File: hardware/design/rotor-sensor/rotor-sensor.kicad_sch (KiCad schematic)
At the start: 48 parts, among them J1 Conn_ARM_SWD_TagConnect_TC203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, J2 Conn_01x06, U4 ATSAMD21E18A-MUT, U5 TLIN1028-Q1, U600 BMI088

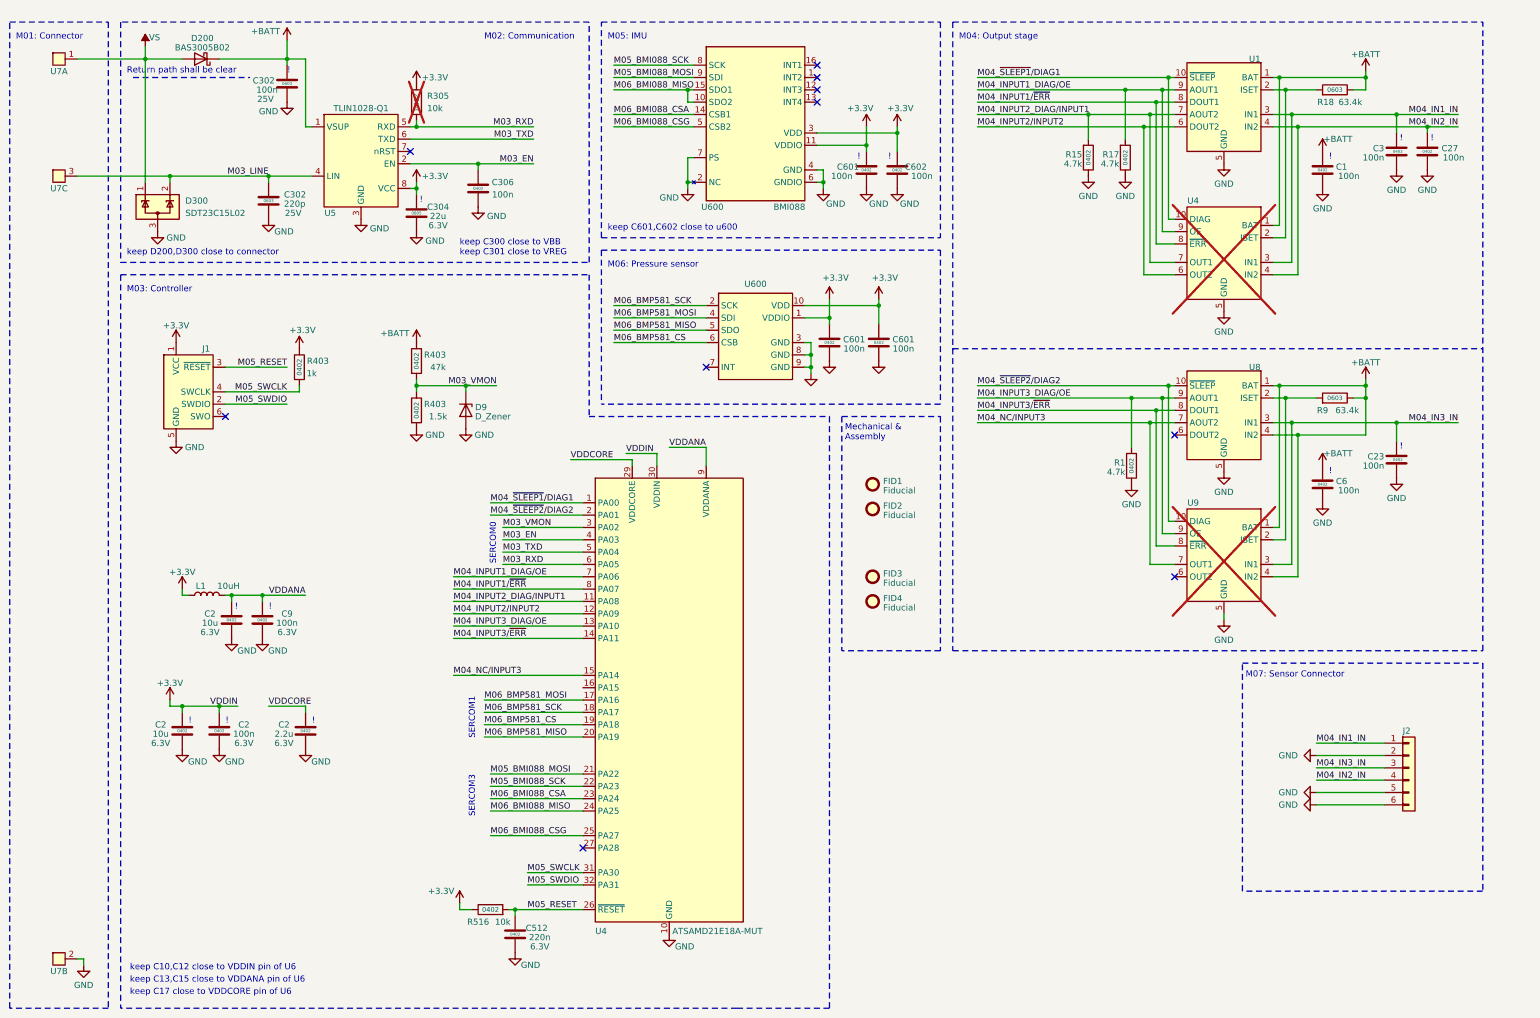
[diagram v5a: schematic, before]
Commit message: FInal ordered hardware
New 3pin connector
Extra 2pin connector for cadence measurement
No 3pin sensor variant
DC/DC converter for MCU
Pressure sensor
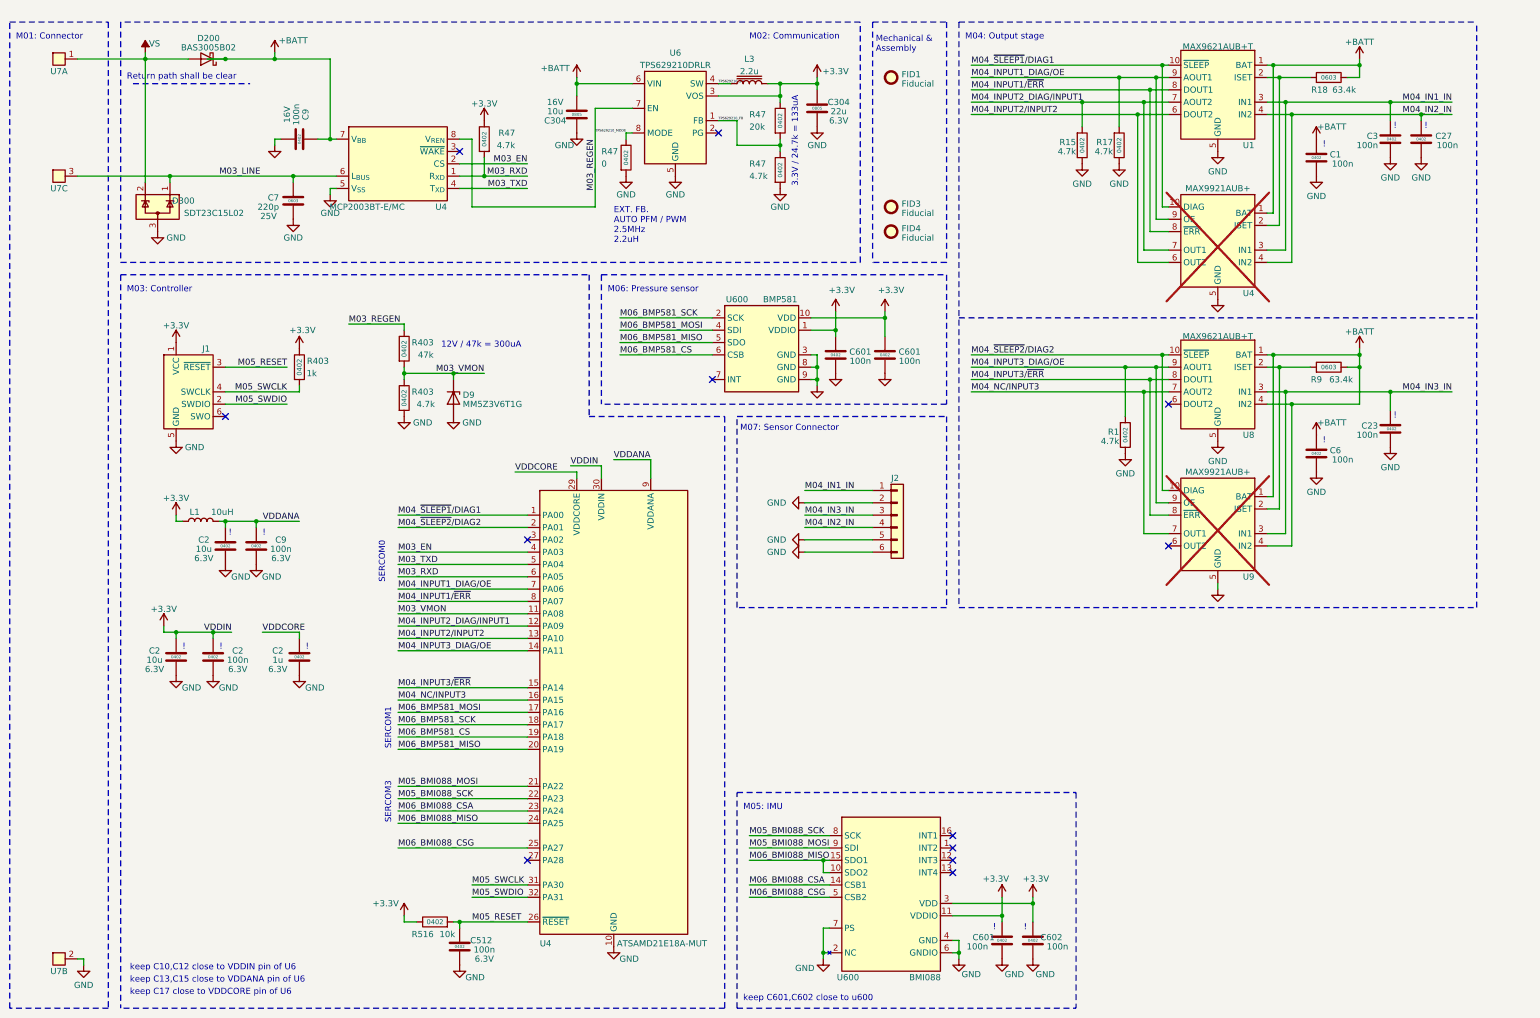
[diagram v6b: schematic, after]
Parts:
- removed C302: 100n, Capacitor_SMD:C_0603_1608Metric, symbol Device:C
- removed C302: 220p, Capacitor_SMD:C_0603_1608Metric, symbol Device:C
- removed C304: 22u, Capacitor_SMD:C_0805_2012Metric, symbol Device:C
- removed C306: 100n, Capacitor_SMD:C_0402_1005Metric, symbol Device:C
- removed FID2: Fiducial, Fiducial:Fiducial_0.5mm_Mask1mm, symbol Mechanical:Fiducial
- removed R305: 10k, Resistor_SMD:R_0402_1005Metric, symbol Device:R
- removed U5: TLIN1028-Q1, Package_SON:Texas_S-PVSON-N8, symbol local_symbols:TLIN1028-Q1
- added C304: 22u, Capacitor_SMD:C_0805_2012Metric, symbol Device:C
- added C304: 10u, Capacitor_SMD:C_0805_2012Metric, symbol Device:C
- added C7: 220p, Capacitor_SMD:C_0603_1608Metric, symbol Device:C
- added C9: 100n, Capacitor_SMD:C_0402_1005Metric, symbol Device:C
- added L3: 2.2u, Inductor_SMD:L_Coilcraft_LPS3010, symbol Device:L_Iron
- added R47: 0, Resistor_SMD:R_0402_1005Metric, symbol Device:R
- added R47: 20k, Resistor_SMD:R_0402_1005Metric, symbol Device:R
- added R47 (x2): 4.7k, Resistor_SMD:R_0402_1005Metric, symbol Device:R
- added U4: MCP2003BT-E/MC, Package_DFN_QFN:DFN-8-1EP_3x2mm_P0.5mm_EP1.7x1.4mm, symbol local:MCP2003
- added U6: TPS629210DRLR, Package_TO_SOT_SMD:SOT-583-8, symbol local_symbols:TPS629210
- C2: value 2.2u -> 1u
- C512: value 220n -> 100n
- D9: value D_Zener -> MM5Z3V6T1G
- R403: value 1.5k -> 4.7k
- U1, U8: value ~ -> MAX9621AUB+T
- U4, U9: value ~ -> MAX9921AUB+
- U600: value ~ -> BMP581
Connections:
- net +3.3V: now also C304.1, L3.2, R47.1, R47.1, U6.3 (VOS)
- net +BATT: now also C304.2, C9.2, U4.7 (V_{BB}), U6.6 (VIN); no longer R403.1
- net GND: now also U4.33 (GND), C304.1, C304.2, C7.2, C9.1, R47.2, R47.2, U4.5 (V_{SS}), U6.5 (GND)
- net M03_EN: now also U4.2 (CS)
- net M03_LINE: now also D300.1 (K), C7.1, U4.6 (L_{BUS}); no longer D300.2 (K)
- net M03_RXD: now also R47.2, U4.1 (R_{XD})
- net M03_TXD: now also U4.4 (T_{XD})
- net M03_VMON: now also U4.11 (PA08); no longer U4.3 (PA02)
- net M04_INPUT2_DIAG/INPUT1: now also U4.12 (PA09); no longer U4.11 (PA08)
- net M04_INPUT2/INPUT2: now also U4.13 (PA10); no longer U4.12 (PA09)
- net M04_INPUT3_DIAG/OE: now also U4.14 (PA11); no longer U4.13 (PA10)
- net M04_INPUT3/~{ERR}: now also U4.15 (PA14); no longer U4.14 (PA11)
- net M04_NC/INPUT3: now also U4.16 (PA15); no longer U4.15 (PA14)
- net VS: now also D300.2 (K); no longer D300.1 (K)
- new net M03_REGEN: R403.1, U4.8 (V_{REN}), U6.7 (EN)
- new net TPS629210_FB: R47.1, R47.2, U6.1 (FB)
- new net TPS629210_MODE: R47.1, U6.8 (MODE)
- new net TPS629210_SW: L3.1, U6.4 (SW)
- no-connect marks 10 -> 12
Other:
- note added: "12V / 47k = 300uA"
- note added: "3.3V / 24.7k = 133uA"
- note added: "EXT. FB. AUTO PFM / PWM 2.5MHz 2.2uH"
- note removed: "keep C300 close to VBB keep C301 close to VREG"
- note removed: "keep D200,D300 close to connector"
- moved on the sheet: C1, C2, C23, C27, C3, C512, C6, C601, C602, C9, D200, D9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
